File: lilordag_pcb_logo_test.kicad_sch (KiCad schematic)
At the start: 112 parts, among them J1 USB4105-GF-A, Q1 MMBT3906, Q2 BC846, Q3 MMBT3906, Q4 BC846, Q5 BC846, Q6 BC846, SW1 PCM12SMTR

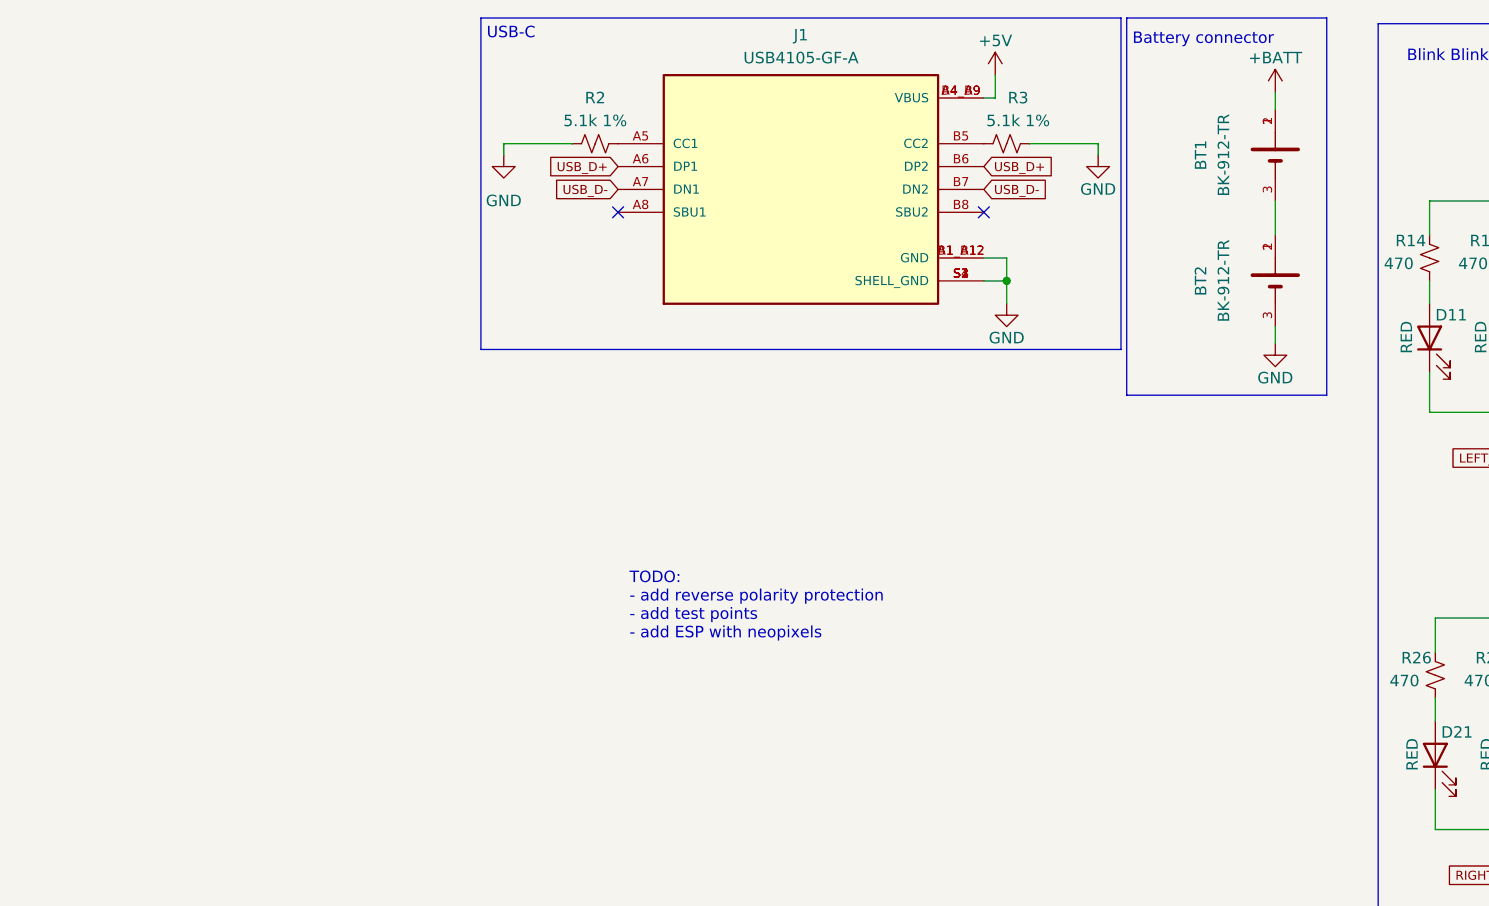
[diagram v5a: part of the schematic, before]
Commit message: Added reverse polarity protection.
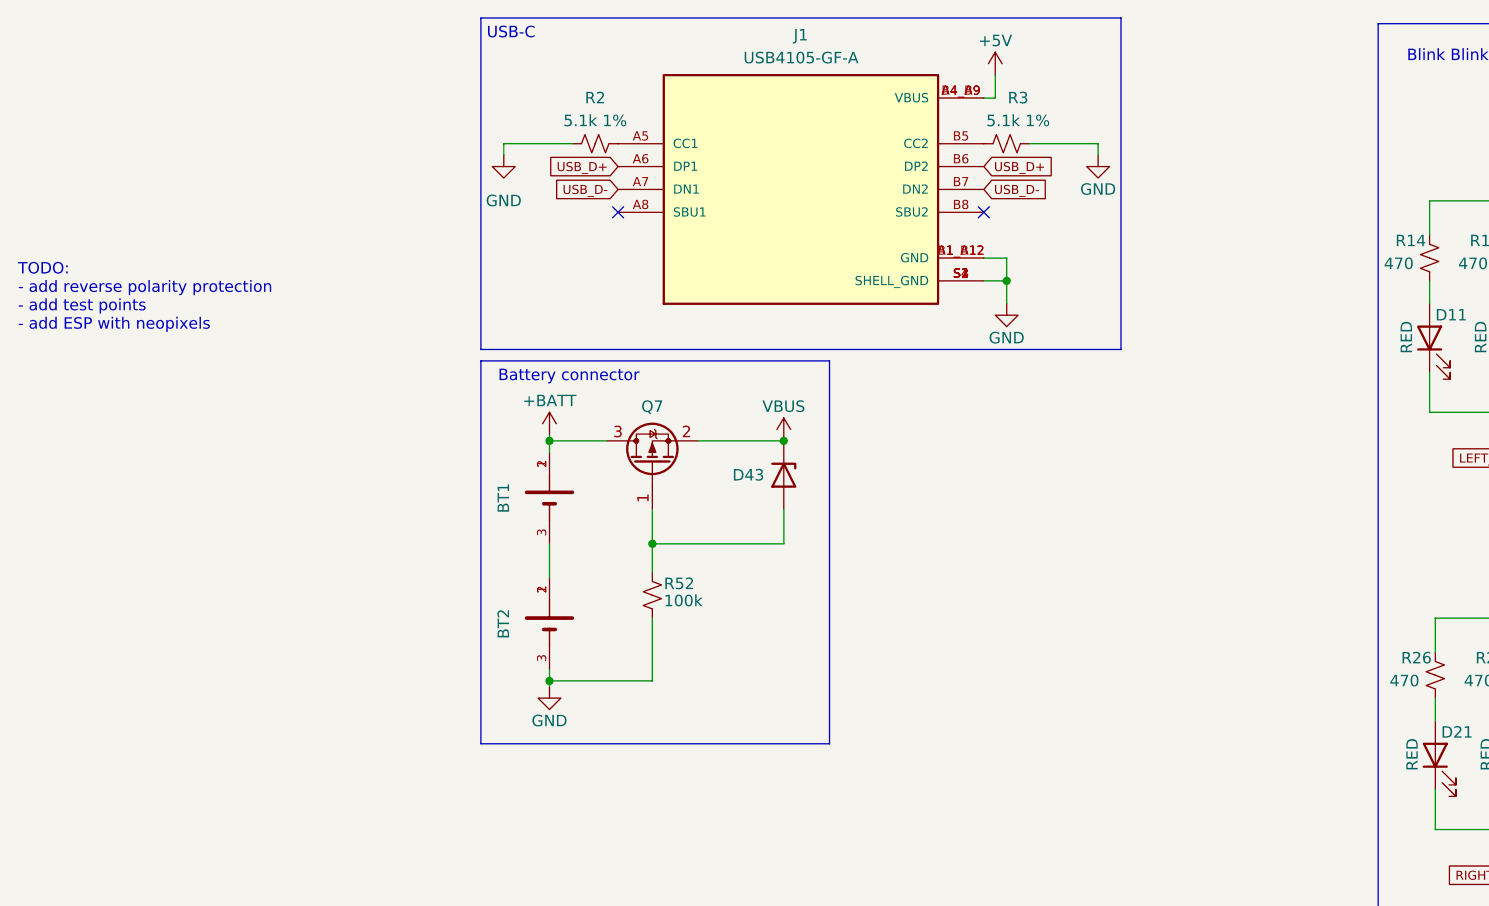
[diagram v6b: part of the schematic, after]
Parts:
- added D43: MMSZ5233B 6V, Diode_SMD:D_SOD-123, symbol Device:D_Zener
- added Q7: SSM3J56MFV, Package_TO_SOT_SMD:SOT-723, symbol Device:Q_PMOS_GSD
- added R52: 100k, Resistor_SMD:R_0603_1608Metric_Pad0.98x0.95mm_HandSolder, symbol Device:R_Small_US
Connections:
- net +BATT: now also Q7.3 (D)
- net GND: now also R52.2
- new net: D43.2 (A), Q7.1 (G), R52.1
- new net VBUS: D43.1 (K), Q7.2 (S)
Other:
- moved on the sheet: BT1, BT2

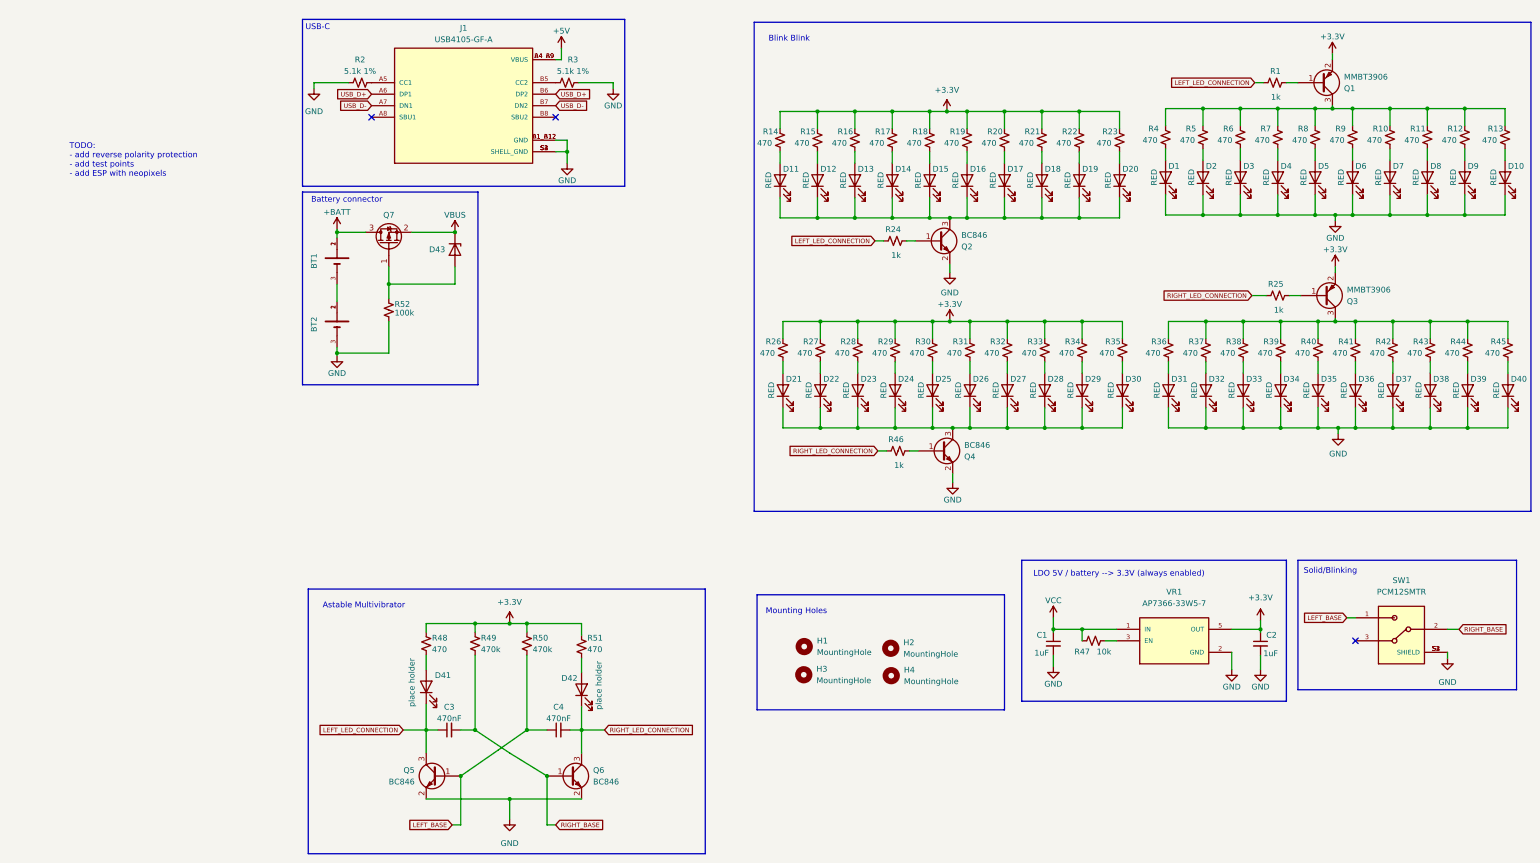
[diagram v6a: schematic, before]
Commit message: Added selector between battery and USB.
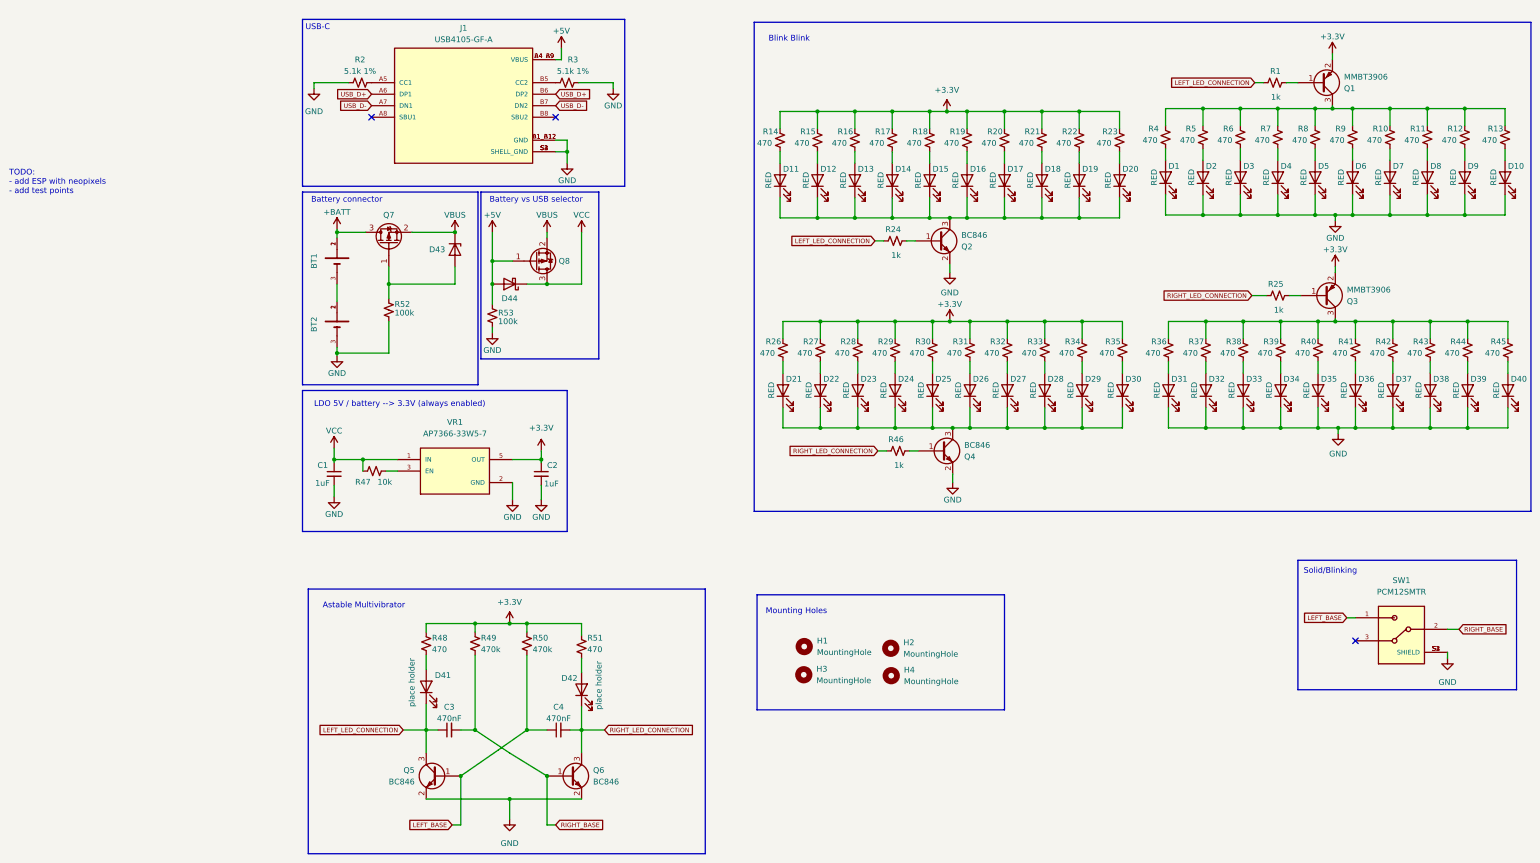
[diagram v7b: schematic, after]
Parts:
- added D44: D_Schottky, Diode_SMD:D_SOD-123F, symbol Device:D_Schottky
- added Q8: SSM3J56MFV, Package_TO_SOT_SMD:SOT-723, symbol Device:Q_PMOS_GSD
- added R53: 100k, Resistor_SMD:R_0603_1608Metric_Pad0.98x0.95mm_HandSolder, symbol Device:R_Small_US
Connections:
- net +5V: now also D44.2 (A), Q8.1 (G), R53.1
- net GND: now also R53.2
- net VBUS: now also Q8.2 (S)
- net VCC: now also D44.1 (K), Q8.3 (D)
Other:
- note added: "Battery vs USB selector"
- note added: "TODO: - add ESP with neopixels - add test points"
- note removed: "TODO: - add reverse polarity protection - add test points - add ESP with neopixels"
- moved on the sheet: C1, C2, R47, VR1

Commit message: Added an on-off switch to the battery.
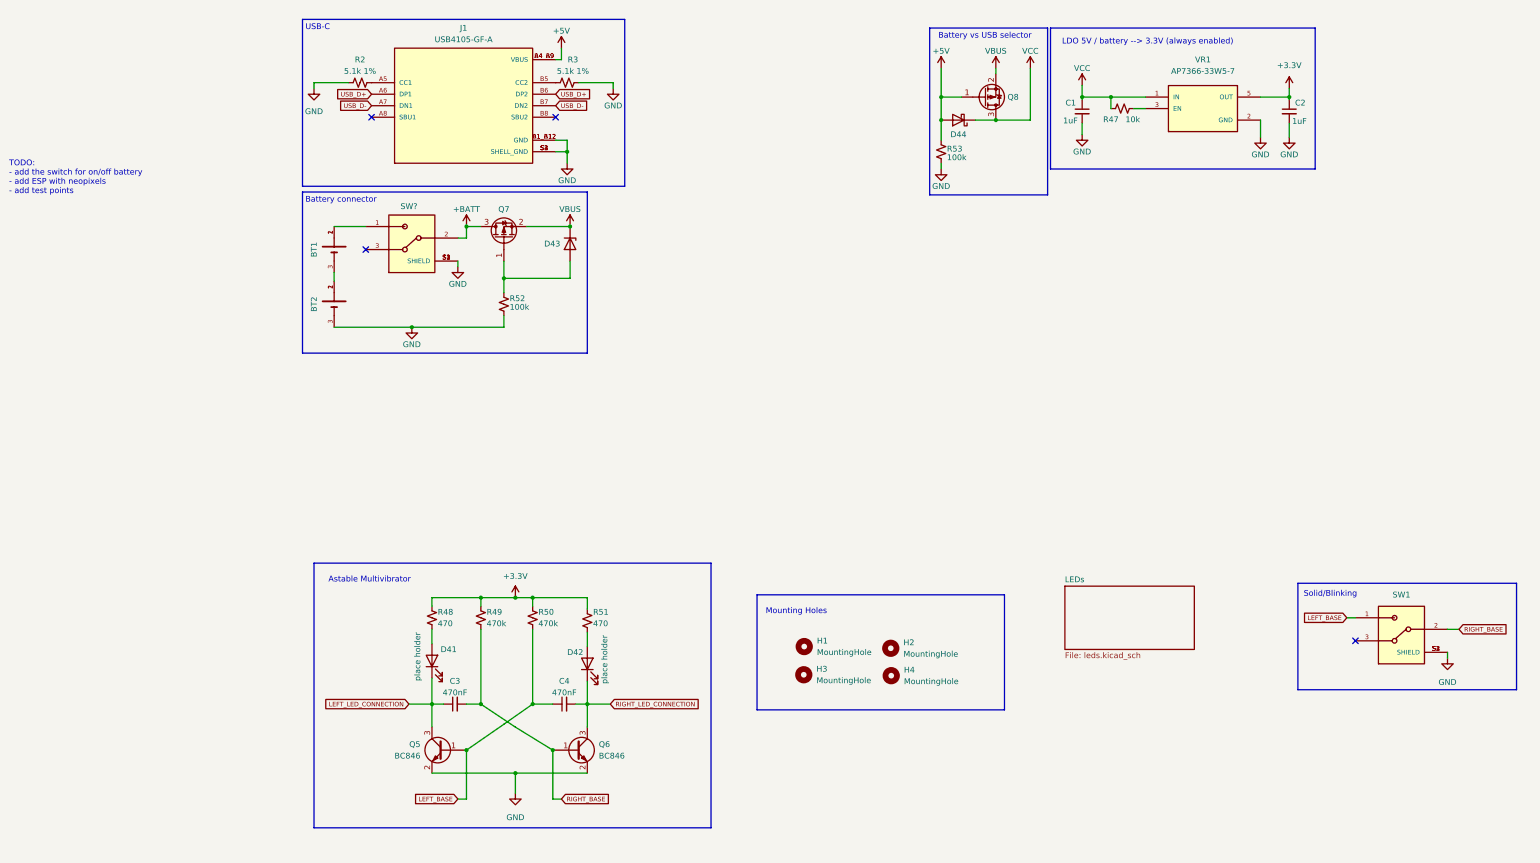
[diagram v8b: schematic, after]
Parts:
- removed D1, D10, D11, D12, D13, D14, D15, D16, D17, D18, D19, D2, D20, D21, D22, D23, D24, D25, D26, D27, D28, D29, D3, D30, D31, D32, D33, D34, D35, D36, D37, D38, D39, D4, D40, D5, D6, D7, D8, D9: RED, LED_SMD:LED_0603_1608Metric_Pad1.05x0.95mm_HandSolder, symbol Device:LED
- removed Q1, Q3: MMBT3906, Package_TO_SOT_SMD:SOT-23, symbol Transistor_BJT:MMBT3906
- removed Q2, Q4: BC846, Package_TO_SOT_SMD:SOT-23, symbol Transistor_BJT:BC846
- removed R1, R24, R25, R46: 1k, Resistor_SMD:R_0603_1608Metric_Pad0.98x0.95mm_HandSolder, symbol Device:R_Small_US
- removed R10, R11, R12, R13, R14, R15, R16, R17, R18, R19, R20, R21, R22, R23, R26, R27, R28, R29, R30, R31, R32, R33, R34, R35, R36, R37, R38, R39, R4, R40, R41, R42, R43, R44, R45, R5, R6, R7, R8, R9: 470, Resistor_SMD:R_0603_1608Metric_Pad0.98x0.95mm_HandSolder, symbol Device:R_Small_US
- added SW?: PCM12SMTR, PCM12SMTR:SW_PCM12SMTR, symbol PCM12SMTR:PCM12SMTR
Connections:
- net +BATT: now also SW?.2; no longer BT1.1, BT1.2
- net GND: now also SW?.S1 (SHIELD), SW?.S2 (SHIELD), SW?.S3 (SHIELD), SW?.S4 (SHIELD)
- new net: BT1.1, BT1.2, SW?.1
- no-connect marks 3 -> 4
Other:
- added sheet LEDs (leds.kicad_sch)
- note added: "TODO: - add the switch for on/off battery - add ESP with neopixels - add test points"
- note removed: "Blink Blink"
- note removed: "TODO: - add ESP with neopixels - add test points"
- moved on the sheet: BT1, BT2, C1, C2, C3, C4, D41, D42, D43, D44, Q5, Q6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
